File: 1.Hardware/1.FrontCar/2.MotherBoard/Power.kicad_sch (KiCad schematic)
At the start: 39 parts

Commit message: update .gitignore
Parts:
- removed C?: 470uF, symbol Device:C_Polarized_Small_US
- removed D? (x2): 1N4148, Diode_SMD:D_SMA, symbol Simulation_SPICE:DIODE
- removed D?: LED, symbol Device:LED
- removed Q?: FMMT619, Package_TO_SOT_SMD:SOT-23, symbol Device:Q_NPN_BEC
- removed Q?: AO4803A, SOIC127P600X175-8N, symbol ErBW_s:AO4803A
- removed R? (x3): 10K, Resistor_SMD:R_1206_3216Metric_Pad1.30x1.75mm_HandSolder, symbol Device:R_Small
- removed R?: 0R, Resistor_SMD:R_1206_3216Metric_Pad1.30x1.75mm_HandSolder, symbol Device:R_Small
- removed R?: 1K, Resistor_SMD:R_1206_3216Metric_Pad1.30x1.75mm_HandSolder, symbol Device:R_Small
- removed SW?: 3x4, ErBW_s:BUTTON_3x4, symbol Switch:SW_Push
- added C?: 470uF, symbol Device:C_Polarized_Small_US
- added C? (x3): (no value), symbol Device:C_Small
- added D?: LED, symbol Device:LED
- added D?: 1N4148, Diode_SMD:D_SMA, symbol Simulation_SPICE:DIODE
- added R?: 5K1, symbol Device:R_Small
- added R? (x3): (no value), Resistor_SMD:R_1206_3216Metric_Pad1.30x1.75mm_HandSolder, symbol Device:R_Small
- added R?: 0R, Resistor_SMD:R_1206_3216Metric_Pad1.30x1.75mm_HandSolder, symbol Device:R_Small
- added SW?: SW_DPDT, symbol Switch:SW_DPDT_x2
- added TP?: GND, TestPoint:TestPoint_Pad_2.5x2.5mm, symbol Connector:TestPoint
- added U?: (no value), symbol ErBW_s:RT9013-33GB
- C? (x4): value 0.1uF -> (none)
- C? (x3): value 22uF -> (none)
- C? (x3): value 10uF -> (none)
- D? (x2): value LED -> (none)
- R? (x2): value 5K1 -> (none)
- R?: value 1K -> (none)
- TP?: value 6V -> (none); footprint TestPoint:TestPoint_Pad_D2.5mm -> (none)
- TP?: value GND -> (none); footprint TestPoint:TestPoint_Pad_2.5x2.5mm -> (none)
- TP?: value 3V3 -> (none); footprint TestPoint:TestPoint_Pad_D2.5mm -> (none)
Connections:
- net GND: now also R?.2; no longer TP?.1
- net GNDPWR: now also C?.2, C?.2, C?.2, C?.2, D?.1 (K), R?.1, R?.2, TP?.1, U?.2 (GND)
- net VBUS: now also SW?.2 (B)
- net VCC: now also D?.2 (K), R?.1
- net +3V3 renamed 3.3V
- net +5V renamed 5V
- net 5V: now also U?.1 (VIN), U?.3 (EN)
- net +6V renamed SERVO_6V
- new net: D?.2 (A), R?.2
- new net: C?.1, U?.4 (NC)
- new net: R?.1, R?.1, R?.2
- new net BATTERY: R?.2
- new net CAM_3.3V: C?.1, C?.1, R?.1, TP?.1, U?.5 (VOUT)
- new net MOTOR_PWR: C?.1, D?.1 (A), SW?.1 (A)
- no-connect marks 4 -> 1
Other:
- note added: "Copyright (c) 2023, ErBW_s All rights reserved."
- note removed: "Copyright (c) 2022, ErBW_s All rights reserved."
- moved on the sheet: C?, D?, R?, RV?, TP?, U?

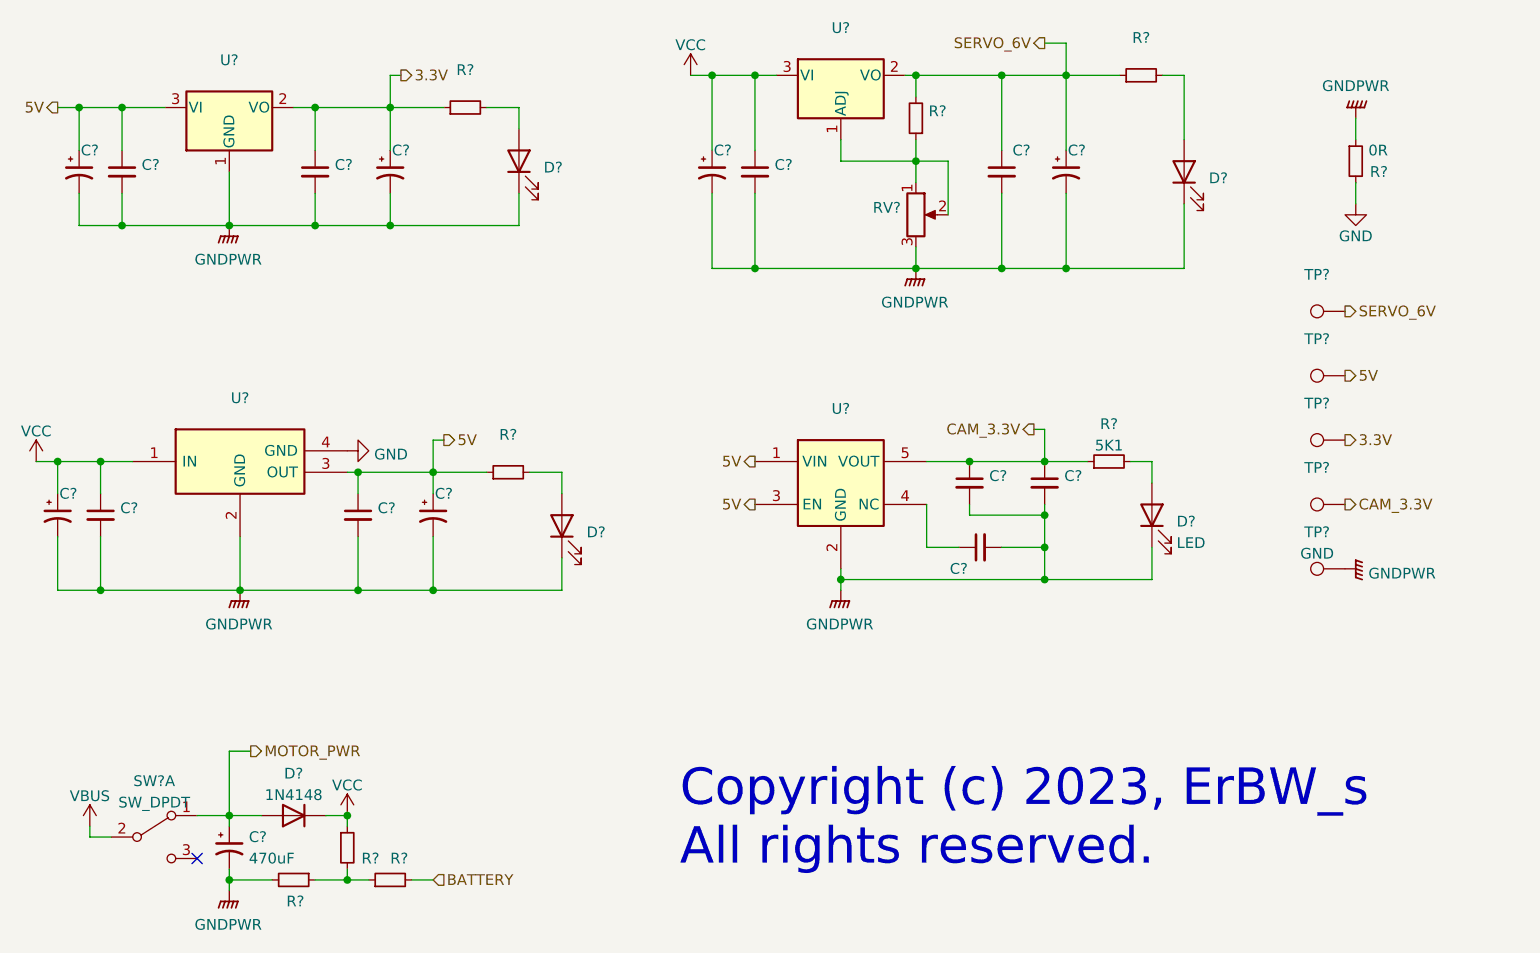
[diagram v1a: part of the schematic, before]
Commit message: 母板原理图完成
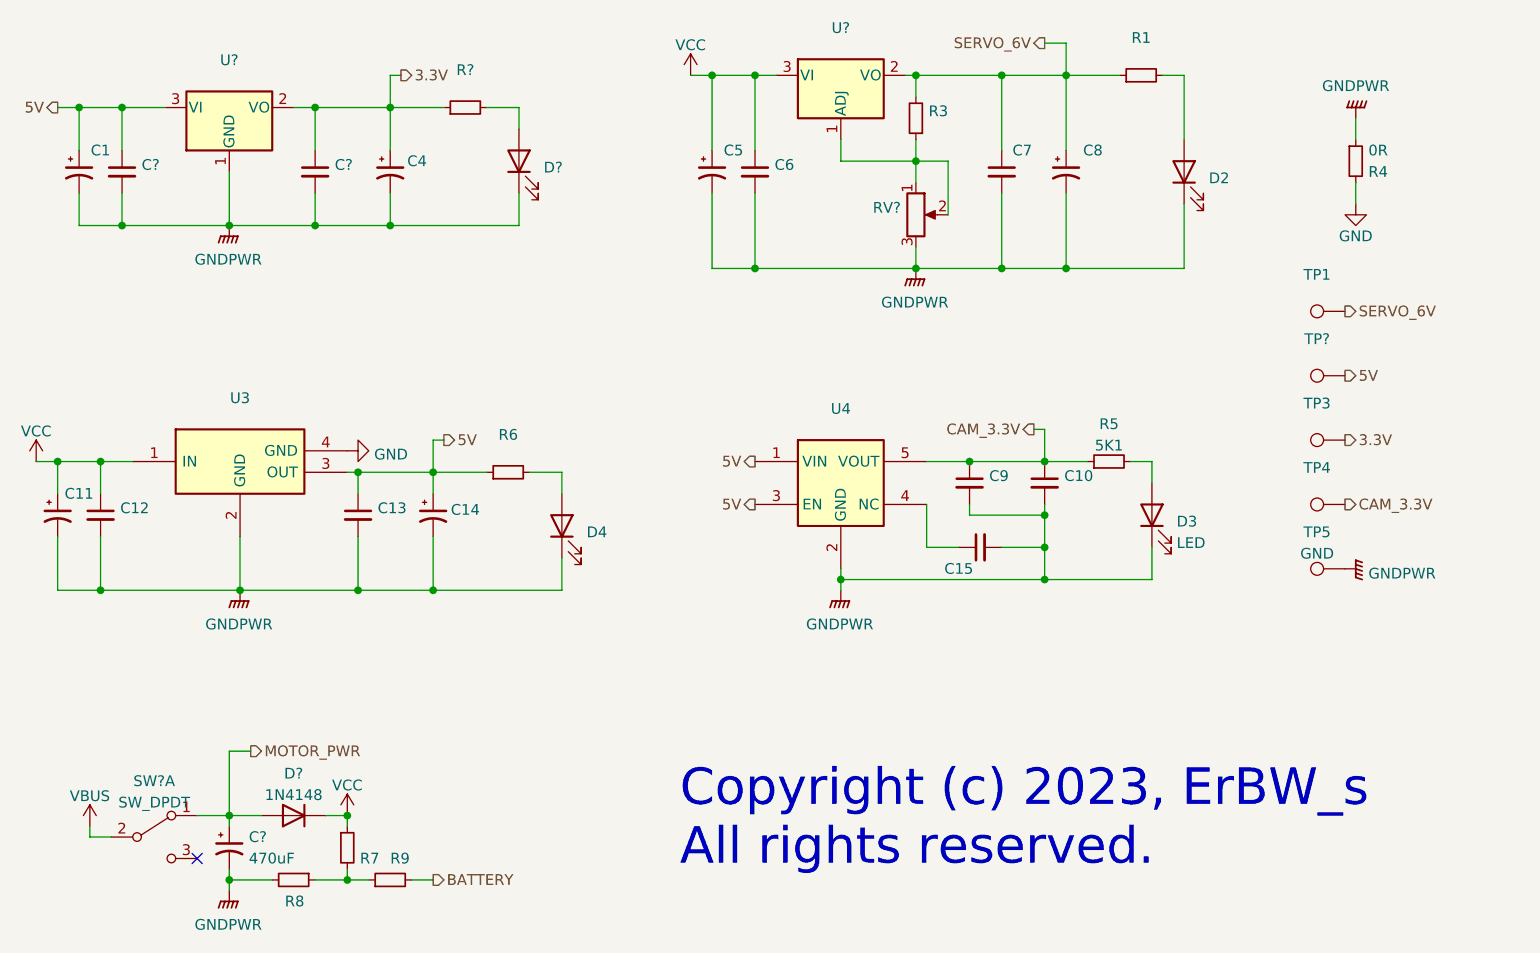
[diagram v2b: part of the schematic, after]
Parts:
- removed U?: LM2940S-5.0, symbol Regulator_Linear:LM2940S-5.0
- added U3: (no value), symbol ErBW_s:LM2940S-5.0
- gave numbers to parts that had none: 29
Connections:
- net 5V: now also U3.3 (OUT)
- net GND: now also U3.4 (GND)
- net GNDPWR: now also U3.2 (GND)
- net VCC: now also U3.1 (IN)

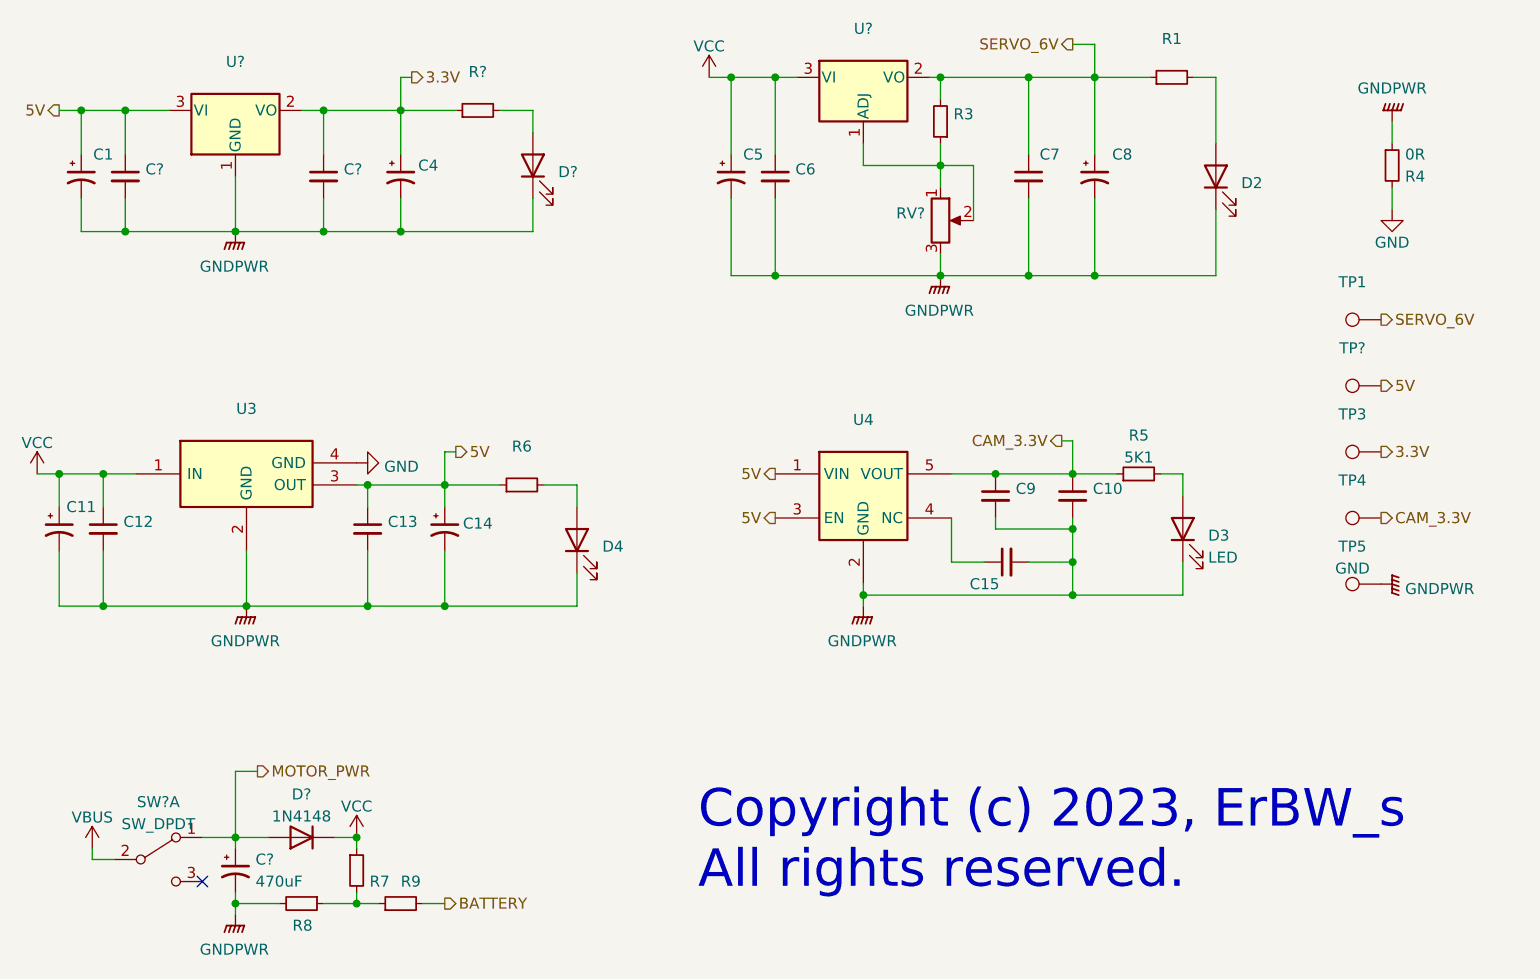
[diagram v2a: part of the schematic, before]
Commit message: 更新母板原理图封装
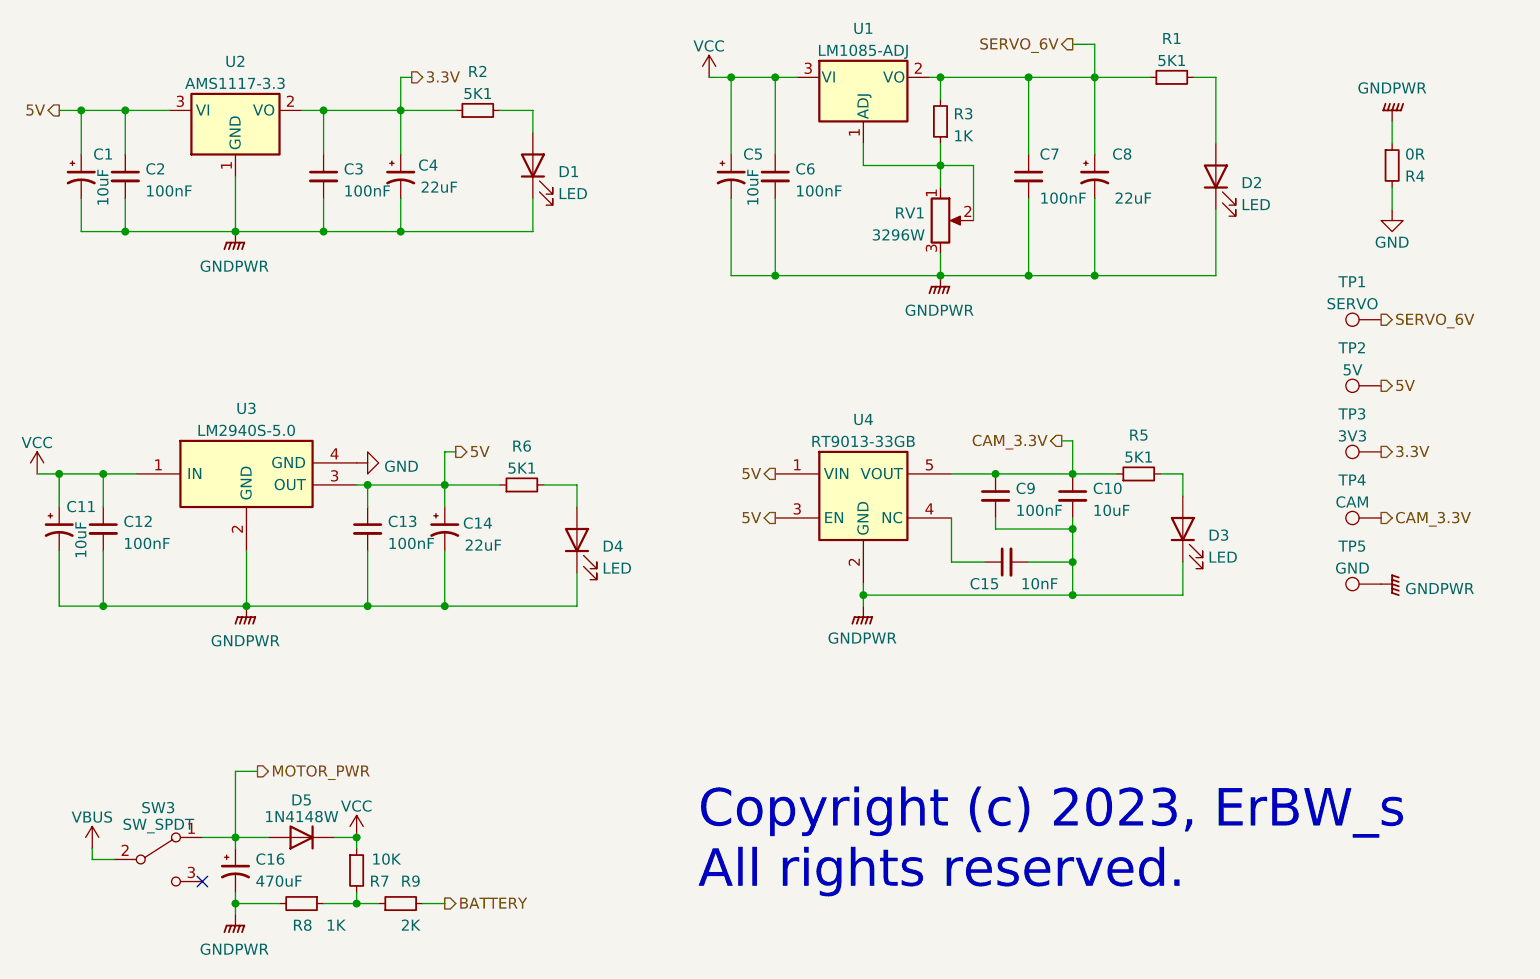
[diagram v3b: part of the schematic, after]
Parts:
- removed D?: 1N4148, Diode_SMD:D_SMA, symbol Simulation_SPICE:DIODE
- removed SW?: SW_DPDT, symbol Switch:SW_DPDT_x2
- added D5: 1N4148W, Diode_SMD:D_SOD-123, symbol Diode:1N4148W
- added SW3: SW_SPDT, ErBW_s:SPDT_MTS_102, symbol Switch:SW_SPDT
- C1, C11, C5: value (none) -> 10uF; footprint (none) -> Capacitor_Tantalum_SMD:CP_EIA-3528-15_AVX-H
- C10: value (none) -> 10uF; footprint (none) -> Capacitor_SMD:C_0603_1608Metric
- C12, C13, C6, C7, C9: value (none) -> 100nF; footprint (none) -> Capacitor_SMD:C_0603_1608Metric
- C14, C4, C8: value (none) -> 22uF; footprint (none) -> Capacitor_Tantalum_SMD:CP_EIA-3528-15_AVX-H
- C15: value (none) -> 10nF; footprint (none) -> Capacitor_SMD:C_0603_1608Metric
- C16: renamed from C?; footprint (none) -> Capacitor_Tantalum_SMD:CP_EIA-7343-30_AVX-N
- C2, C3: renamed from C?; footprint (none) -> Capacitor_SMD:C_0603_1608Metric
- D1: renamed from D?; footprint (none) -> LED_SMD:LED_0805_2012Metric
- D2, D4: value (none) -> LED; footprint (none) -> LED_SMD:LED_0805_2012Metric
- D3: footprint (none) -> LED_SMD:LED_0805_2012Metric
- R1, R6: value (none) -> 5K1; footprint (none) -> Resistor_SMD:R_0603_1608Metric
- R2: renamed from R?; footprint (none) -> Resistor_SMD:R_0603_1608Metric
- R3: value (none) -> 1K; footprint (none) -> Resistor_SMD:R_0603_1608Metric
- R5: footprint (none) -> Resistor_SMD:R_0603_1608Metric
- R7: value (none) -> 10K; footprint Resistor_SMD:R_1206_3216Metric_Pad1.30x1.75mm_HandSolder -> Resistor_SMD:R_0603_1608Metric
- R8: value (none) -> 1K; footprint Resistor_SMD:R_1206_3216Metric_Pad1.30x1.75mm_HandSolder -> Resistor_SMD:R_0603_1608Metric
- R9: value (none) -> 2K; footprint Resistor_SMD:R_1206_3216Metric_Pad1.30x1.75mm_HandSolder -> Resistor_SMD:R_0603_1608Metric
- RV1: renamed from RV?; footprint (none) -> ErBW_s:3296W
- TP1: value (none) -> SERVO; footprint (none) -> TestPoint:TestPoint_Pad_D2.5mm
- TP3: value (none) -> 3V3; footprint (none) -> TestPoint:TestPoint_Pad_D2.5mm
- TP4: value (none) -> CAM; footprint (none) -> TestPoint:TestPoint_Pad_2.5x2.5mm
- U3: value (none) -> LM2940S-5.0; footprint (none) -> Package_TO_SOT_SMD:TO-263-3_TabPin4
- U4: value (none) -> RT9013-33GB; footprint (none) -> Package_TO_SOT_SMD:SOT-23-5
- gave numbers to parts that had none: 3
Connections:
- net MOTOR_PWR: now also D5.2 (A), SW3.1 (A)
- net VBUS: now also SW3.2 (B)
- net VCC: now also D5.1 (K)

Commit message: 母板pcb初步排布
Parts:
- TP4, TP5: footprint TestPoint:TestPoint_Pad_2.5x2.5mm -> TestPoint:TestPoint_Pad_D2.5mm
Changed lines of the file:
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@@
       (effects (font (size 1.27 1.27)))
     )
-    (property "Footprint" "TestPoint:TestPoint_Pad_2.5x2.5mm" (at 177.8 69.85 0)
+    (property "Footprint" "TestPoint:TestPoint_Pad_D2.5mm" (at 177.8 69.85 0)
       (effects (font (size 1.27 1.27)) hide)
     )
@@
       (effects (font (size 1.27 1.27)))
     )
-    (property "Footprint" "TestPoint:TestPoint_Pad_2.5x2.5mm" (at 177.8 77.47 0)
+    (property "Footprint" "TestPoint:TestPoint_Pad_D2.5mm" (at 177.8 77.47 0)
       (effects (font (size 1.27 1.27)) hide)
     )
